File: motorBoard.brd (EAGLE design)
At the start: 70 x 25 mm, 20 parts, among them IC1 PIC18F4XK22PT

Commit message: modified text
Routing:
- net GND: track 121.5 -> 122.3 mm
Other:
- board text added: "Motor Controller"
- board text added: "v1.0 (2015)"
- board text removed: "Motor board v1.0 (2015)"

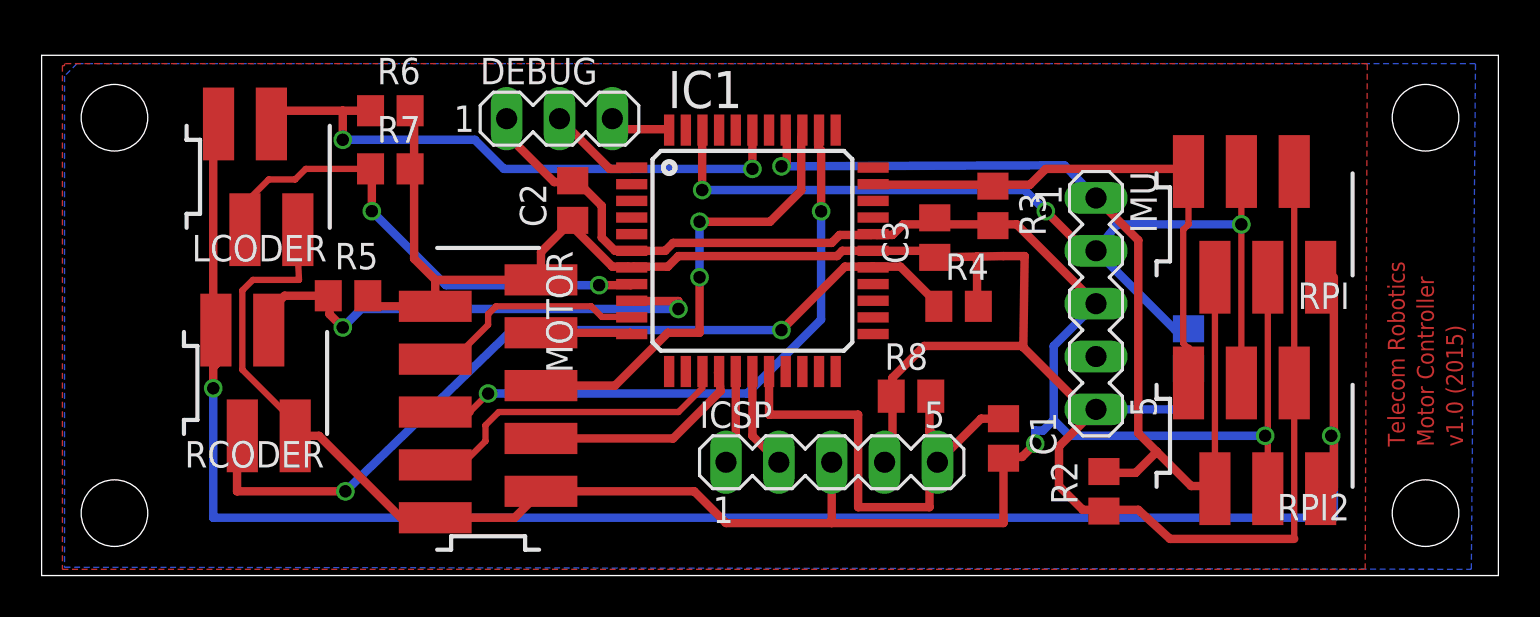
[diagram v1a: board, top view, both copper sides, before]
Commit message: added power and status LEDs, fixed silkscreen
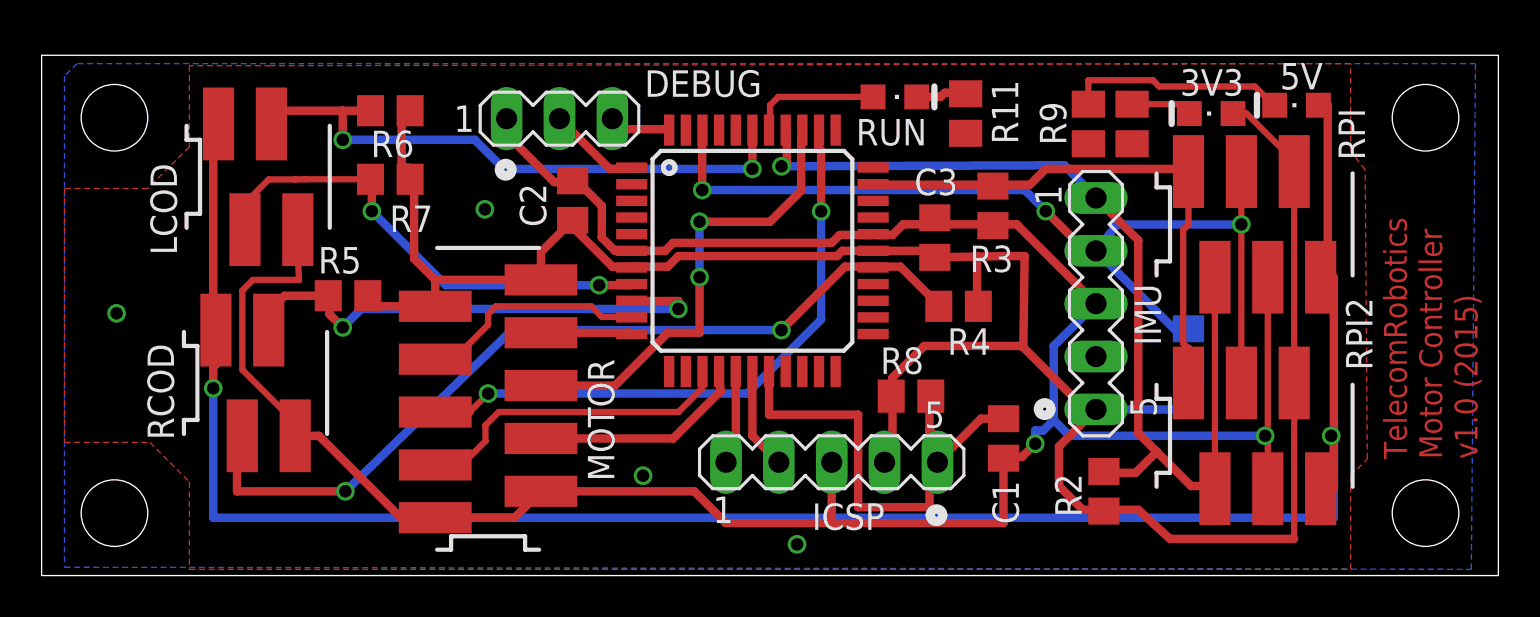
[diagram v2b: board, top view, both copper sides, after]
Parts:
- added 3V3, 5V, RUN: (no value), adafruit:CHIPLED_0805
- added R10, R11: 4.7k, resistor:M0805
- added R9: 10k, resistor:M0805
- moved R7 0.50 mm to (16.8, 19.0)
- renumbered LCODER to LCOD, RCODER to RCOD
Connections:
- new net N$10: 5V.C, R9.1
- new net N$14: 3V3.C, R10.1
- new net N$15: IC1.38, RUN.A
- new net N$9: R11.1, RUN.C
- net GND: now also R10.2, R11.2, R9.2
- net VCC: now also 3V3.A
- net VDD: now also 5V.A
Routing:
- net N$10: track 0.00 -> 10.6 mm
- net VDD: track 87.9 -> 97.6 mm
- net N$15: track 0.00 -> 6.32 mm
- net VCC: track 110.8 -> 116.5 mm
- net N$14: track 0.00 -> 3.07 mm
- net N$9: track 0.00 -> 2.48 mm
- net GND: vias 2 -> 6
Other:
- board text added: "TelecomRobotics"
- board text removed: "Telecom Robotics"

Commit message: added some more vias
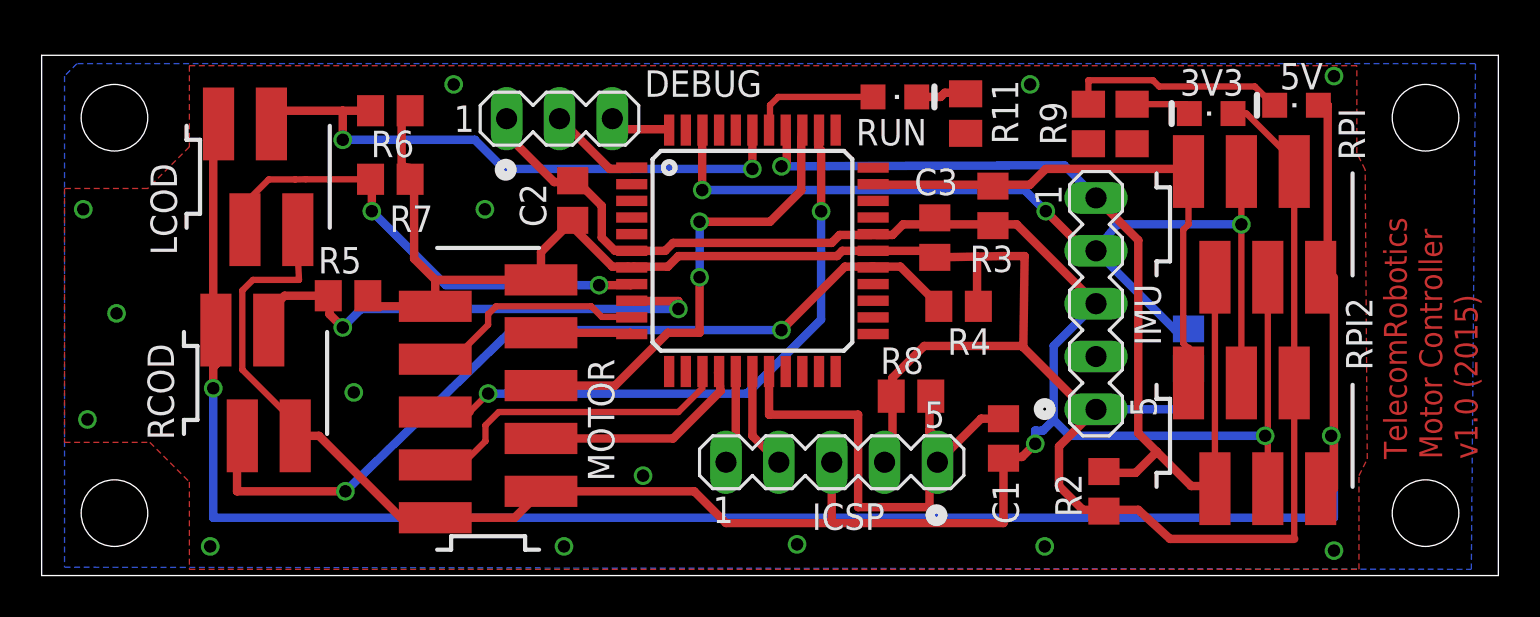
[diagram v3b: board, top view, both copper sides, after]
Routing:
- net GND: vias 6 -> 16
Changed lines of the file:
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@@
 <vertex x="1.7" y="24.6"/>
 </polygon>
-<polygon width="0.4064" layer="1" isolate="0.3048">
-<vertex x="11" y="24.5"/>
+<polygon width="0.3048" layer="1" isolate="0.3048">
+<vertex x="63.2" y="24.5"/>
 <vertex x="7.1" y="24.5"/>
 <vertex x="7.1" y="20.6"/>
@@
 <vertex x="7.1" y="4.5"/>
 <vertex x="7.1" y="0.3"/>
-<vertex x="62.9" y="0.3"/>
-<vertex x="62.9" y="4.8"/>
+<vertex x="63.3" y="0.3"/>
+<vertex x="63.3" y="4.8"/>
 <vertex x="63.7" y="5.6"/>
 <vertex x="63.6" y="19.5"/>
-<vertex x="62.9" y="20.4"/>
-<vertex x="62.9" y="24.6"/>
+<vertex x="63.2" y="20.3"/>
 </polygon>
 <via x="3.6" y="12.6" extent="1-16" drill="0.6"/>
@@
 <via x="21.3" y="17.6" extent="1-16" drill="0.6"/>
 <via x="28.9" y="4.8" extent="1-16" drill="0.6"/>
+<via x="2" y="17.6" extent="1-16" drill="0.6"/>
+<via x="2.2" y="7.5" extent="1-16" drill="0.6"/>
+<via x="8.1" y="1.4" extent="1-16" drill="0.6"/>
+<via x="62.1" y="24" extent="1-16" drill="0.6"/>
+<via x="62.1" y="1.2" extent="1-16" drill="0.6"/>
+<via x="19.8" y="23.6" extent="1-16" drill="0.6"/>
+<via x="47.5" y="23.6" extent="1-16" drill="0.6"/>
+<via x="25.1" y="1.4" extent="1-16" drill="0.6"/>
+<via x="48.2" y="1.4" extent="1-16" drill="0.6"/>
+<via x="15" y="8.8" extent="1-16" drill="0.6"/>
+<wire x1="13.327" y1="6.715" x2="15" y2="8.8" width="0" layer="19" extent="1-1"/>
 </signal>
 <signal name="N$9">
